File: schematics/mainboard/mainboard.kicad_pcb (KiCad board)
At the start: 4 copper layers, 92 x 166.8 mm, 82 parts, among them J1 SD_Card_Receptacle, J2 Conn_02x20_Odd_Even_MountingP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, J3 USB_C_Receptacle_USB2.0_16P, J4 Conn_01x02, J5 Conn_01x03_Pin, J6 Conn_01x12, P1 1-1473005-4, SW1 SW_SPST, U1 AMS1117-3.3, U2 AMS1117-3.3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

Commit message: SD card connector fixed in schematics. Added JLCPBC part numbers to some components.
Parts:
- added R29: 57k, Resistor_SMD:R_0805_2012Metric_Pad1.20x1.40mm_HandSolder, F.Cu at (124.0, 115.8)
- J1: footprint Connector_Card:SD_Hirose_DM1AA_SF_PEJ82 -> DM1AA-SF-PEJ(82):RetroDACK SD_Hirose_DM1AA_SF_PEJ82
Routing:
- net GND: track 183.4 -> 197.5 mm, vias 56 -> 60
- net SD_CARD: track 0.00 -> 4.69 mm
- net 3V3_LCD: track 148.5 -> 151.4 mm

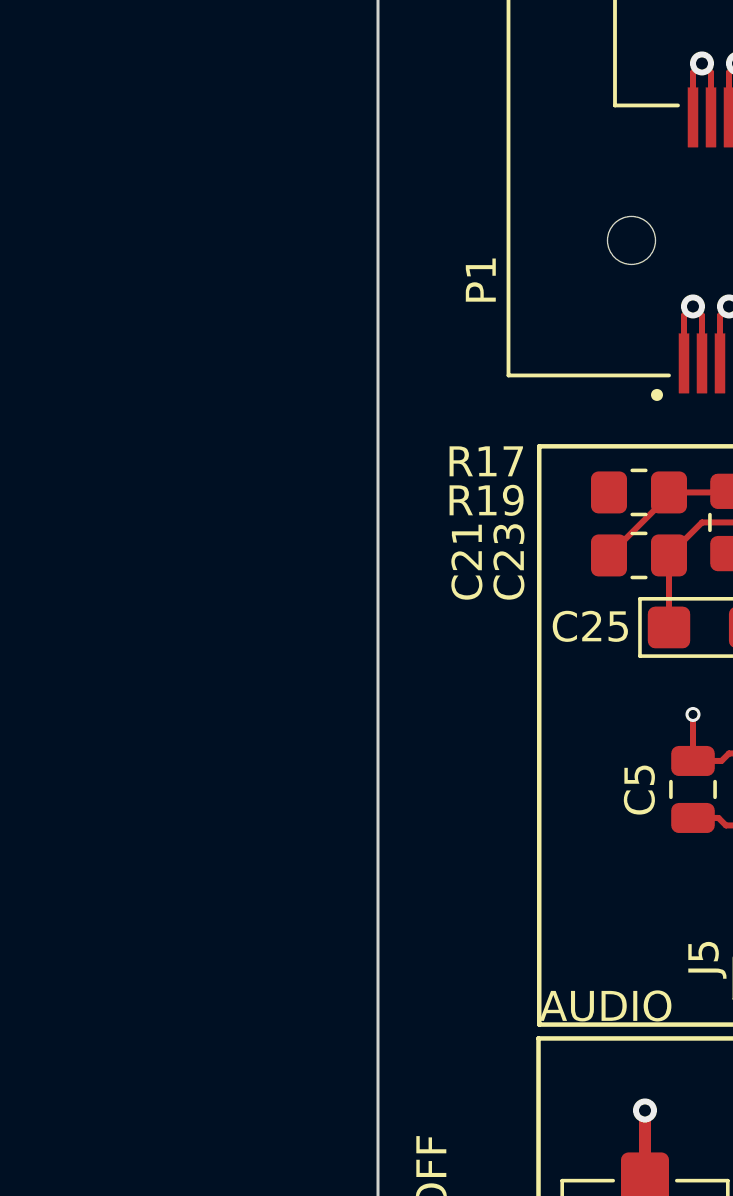
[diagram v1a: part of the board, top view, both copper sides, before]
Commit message: Added connector for trackball to mainboard schematics.
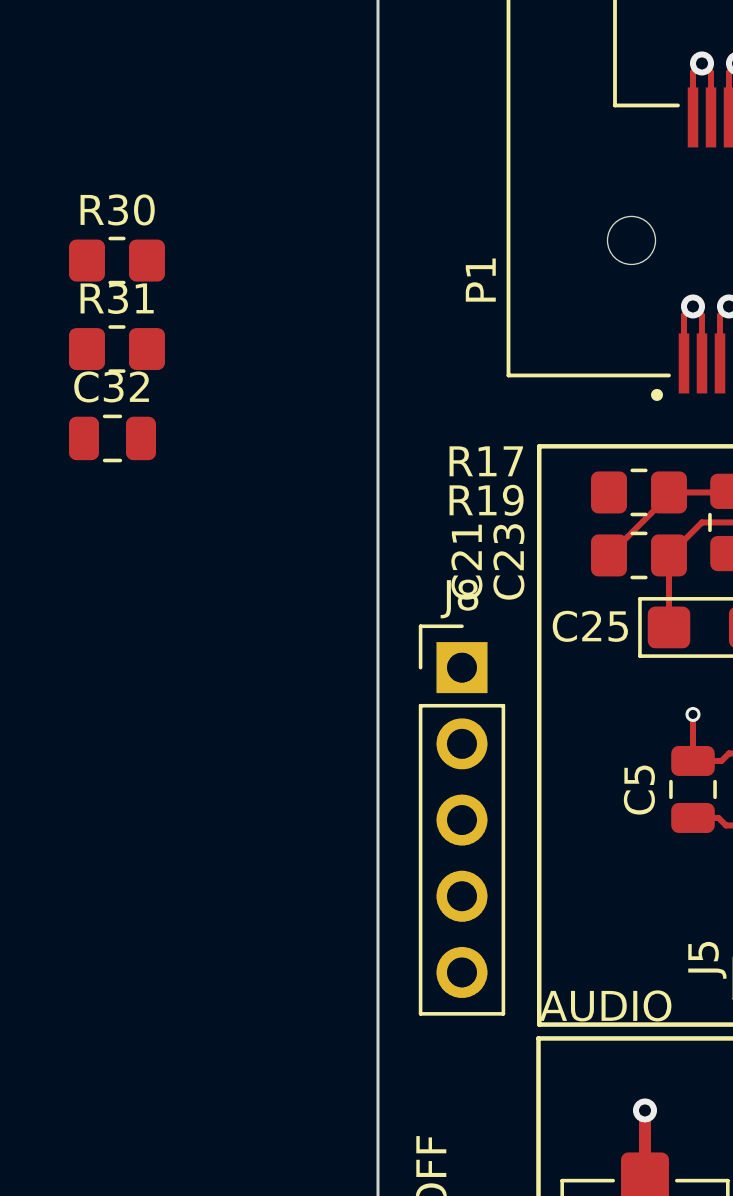
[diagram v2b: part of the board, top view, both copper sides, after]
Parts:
- added C32: 1uF, Capacitor_SMD:C_0805_2012Metric, F.Cu at (106.2, 201.5)
- added J8: TRACKBALL_CONN, Connector_PinHeader_2.54mm:PinHeader_1x05_P2.54mm_Vertical, F.Cu at (117.8, 209.1)
- added R30: 1k2, Resistor_SMD:R_0805_2012Metric_Pad1.20x1.40mm_HandSolder, F.Cu at (106.3, 195.6)
- added R31: 1k2, Resistor_SMD:R_0805_2012Metric_Pad1.20x1.40mm_HandSolder, F.Cu at (106.3, 198.5)
- J2: value Conn_02x20_Odd_Even_MountingPin -> LCD_CONN
- J4: value Conn_01x02 -> BATTERY_CONN
- J6: value Conn_01x12 -> HID_CONN
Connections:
- P1 pad 58: unconnected-(P1-Pad58) -> I2C_SCL
- P1 pad 60: unconnected-(P1-Pad60) -> I2C_SDA
- P1 pad 62: unconnected-(P1-Pad62) -> I2C_INTERRUPT

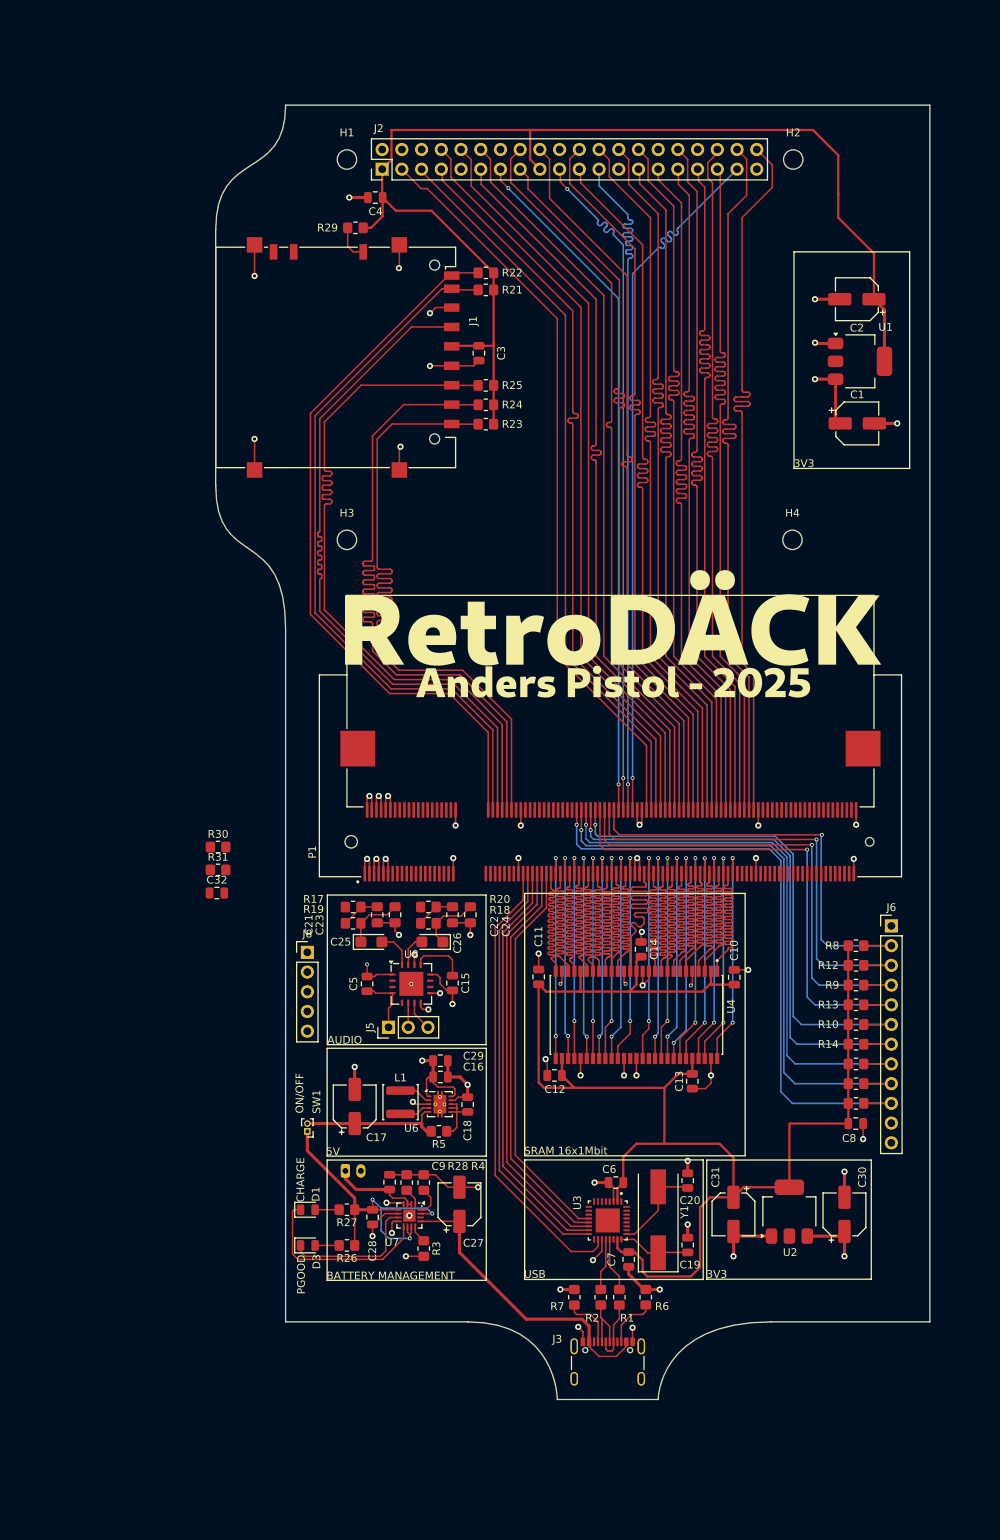
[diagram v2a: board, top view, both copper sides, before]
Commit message: Updated mainboard to use I2S audio.
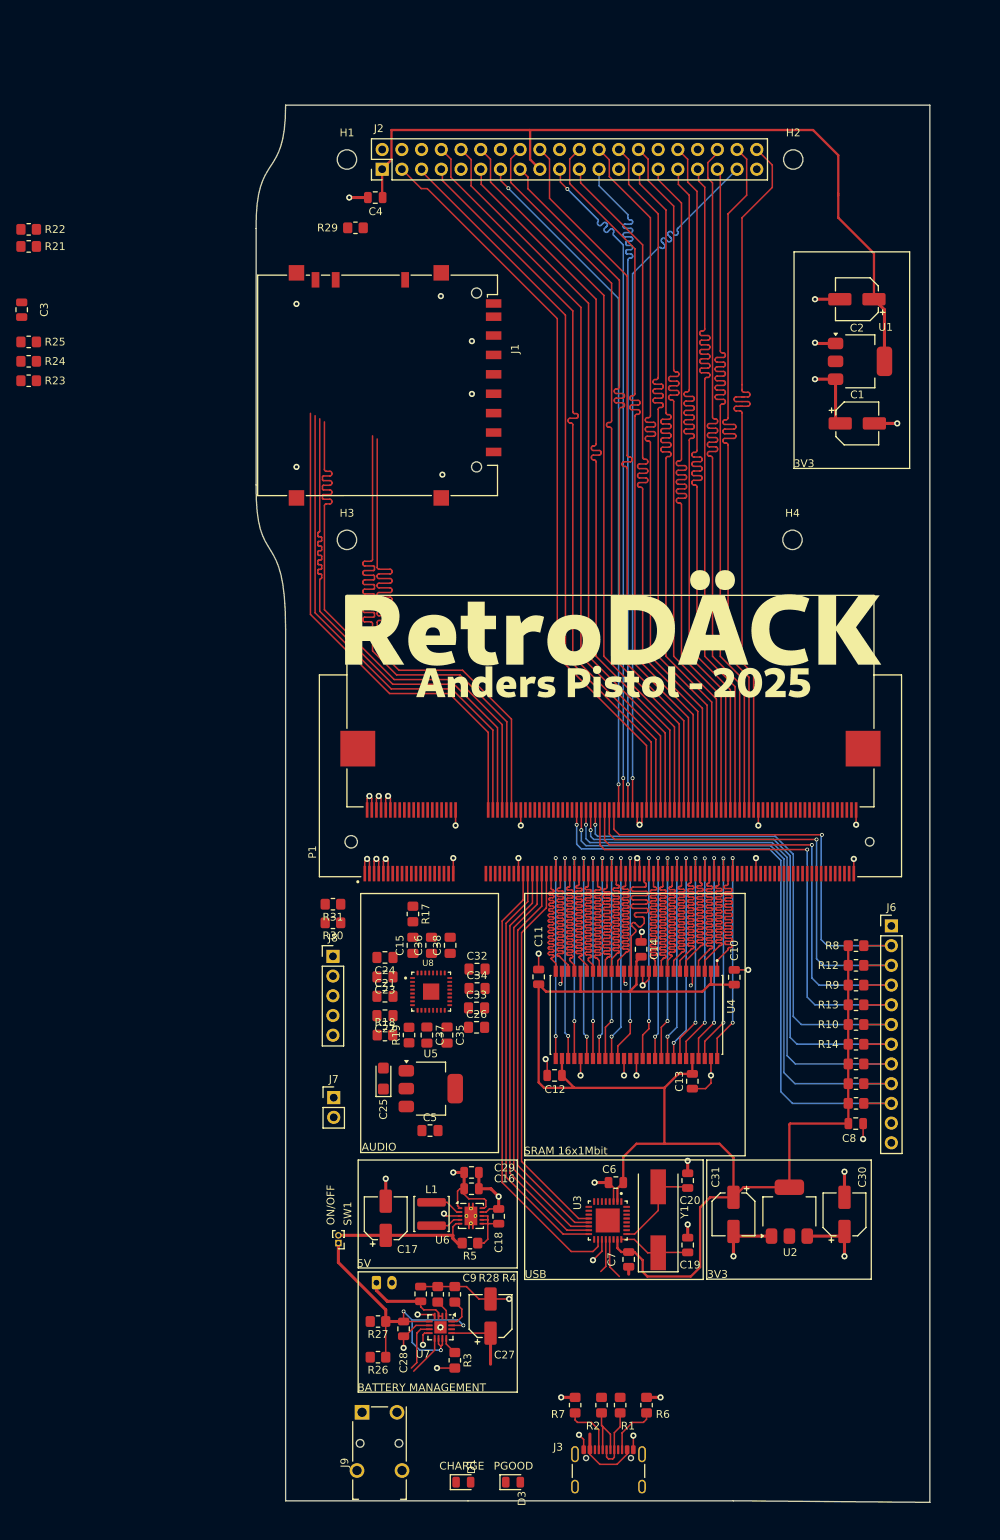
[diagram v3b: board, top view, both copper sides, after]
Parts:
- removed J5: Conn_01x03_Pin, Connector_PinHeader_2.54mm:PinHeader_1x03_P2.54mm_Vertical
- removed R20: 4k7, Resistor_SMD:R_0805_2012Metric_Pad1.20x1.40mm_HandSolder
- added C33: 10uF, Capacitor_SMD:C_0805_2012Metric_Pad1.18x1.45mm_HandSolder, F.Cu at (139.6, 216.3)
- added C34: 22uF, Capacitor_SMD:C_0805_2012Metric_Pad1.18x1.45mm_HandSolder, F.Cu at (139.7, 213.8)
- added C35: 0.1uF, Capacitor_SMD:C_0805_2012Metric_Pad1.18x1.45mm_HandSolder, F.Cu at (135.8, 219.8)
- added C36: 0.1uF, Capacitor_SMD:C_0805_2012Metric_Pad1.18x1.45mm_HandSolder, F.Cu at (133.8, 208.2)
- added C37: 10uF, Capacitor_SMD:C_0805_2012Metric_Pad1.18x1.45mm_HandSolder, F.Cu at (133.2, 219.8)
- added C38: 22uF, Capacitor_SMD:C_0805_2012Metric_Pad1.18x1.45mm_HandSolder, F.Cu at (136.2, 208.2)
- added J7: Conn_01x02_Pin, Connector_PinHeader_2.54mm:PinHeader_1x02_P2.54mm_Vertical, F.Cu at (121.2, 227.9)
- added J9: AudioJack3, Connector_Audio:Jack_3.5mm_Switronic_ST-005-G_horizontal, F.Cu at (127.1, 274.9)
- added U5: AMS1117-1.8, Package_TO_SOT_SMD:SOT-223-3_TabPin2, F.Cu at (133.7, 226.7)
- C15, C32: value 1uF -> 0.1uF; footprint Capacitor_SMD:C_0805_2012Metric -> Capacitor_SMD:C_0805_2012Metric_Pad1.18x1.45mm_HandSolder
- C21, C23: value 10nF -> 0.1uF
- C22, C24: value 10nF -> 10uF
- C26: value 47uF -> 0.1uF; footprint Capacitor_Tantalum_SMD:CP_EIA-3216-18_Kemet-A -> Capacitor_SMD:C_0805_2012Metric_Pad1.18x1.45mm_HandSolder
- C5: value 1uF -> 10uF; footprint Capacitor_SMD:C_0805_2012Metric -> Capacitor_SMD:C_0805_2012Metric_Pad1.18x1.45mm_HandSolder
- U8: value MAX9715xTE+ -> ~; footprint Package_DFN_QFN:TQFN-16-1EP_5x5mm_P0.8mm_EP3.1x3.1mm -> MY_AUDIO:QFN50P500X500X100-33N
- moved C3 59.2 mm to (81.0, 126.3)
- moved R21 59.2 mm to (81.9, 118.2)
- moved R22 59.2 mm to (81.9, 116.0)
- moved R23 59.2 mm to (81.9, 135.5)
- moved R24 59.2 mm to (81.9, 133.0)
- moved R25 59.2 mm to (81.9, 130.5)
- moved D1 40.4 mm to (137.9, 277.4)
- moved D3 40.4 mm to (144.3, 277.4)
- moved C32 34.9 mm to (139.7, 211.3)
- moved C5 20.6 mm to (133.6, 232.1), turned to 0 degrees
- moved R30 17.7 mm to (121.1, 205.3), turned to 180 degrees
- moved C25 17.7 mm to (127.6, 225.4), turned to 90 degrees
- moved R18 17.4 mm to (127.8, 219.8)
- moved R19 16.1 mm to (130.9, 219.8), turned to 90 degrees
- moved C22 15.6 mm to (127.8, 217.3), turned to 180 degrees
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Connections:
- net Net-(U8-OUTR+) renamed VOL/MICDET
- C15 pad 1: Net-(U8-BIAS) -> ~{RESET}
- C2 pad 1: 3V3_LCD -> 3V3_AUDIO
- C21 pad 1: Net-(C21-Pad1) -> 1V8
- C22 pad 1: GND -> 1V8
- C22 pad 2: Net-(C22-Pad2) -> GND
- C23 pad 1: Net-(C23-Pad1) -> 3V3_AUDIO
- C24 pad 1: GND -> 3V3_AUDIO
- C24 pad 2: Net-(C24-Pad2) -> GND
- C25 pad 1: Net-(C23-Pad1) -> 1V8
- C25 pad 2: Net-(U8-INL) -> GND
- C26 pad 1: Net-(C24-Pad2) -> 3V3_AUDIO
- C26 pad 2: Net-(U8-INR) -> GND
- C3 pad 2: 3V3_LCD -> 3V3_AUDIO
- C32 pad 1: GND -> 5V0
- C32 pad 2: 5V0 -> GND
- C4 pad 2: 3V3_LCD -> 3V3_AUDIO
- C5 pad 1: GND -> 3V3_AUDIO
- C5 pad 2: 5V0 -> GND
- J1 pad 4: 3V3_LCD -> 3V3_AUDIO
- J2 pad 1: 3V3_LCD -> 3V3_AUDIO
- J2 pad 17: 3V3_LCD -> 3V3_AUDIO
- R17 pad 1: PWM_L -> 3V3_AUDIO
- R17 pad 2: Net-(C21-Pad1) -> ~{RESET}
- R18 pad 1: PWM_R -> 3V3_AUDIO
- R18 pad 2: Net-(C22-Pad2) -> AUDIO_SDA
- R19 pad 1: Net-(C21-Pad1) -> 3V3_AUDIO
- R19 pad 2: Net-(C23-Pad1) -> AUDIO_SCL
- R21 pad 2: 3V3_LCD -> 3V3_AUDIO
- R22 pad 2: 3V3_LCD -> 3V3_AUDIO
- R23 pad 2: 3V3_LCD -> 3V3_AUDIO
- R24 pad 2: 3V3_LCD -> 3V3_AUDIO
- R25 pad 2: 3V3_LCD -> 3V3_AUDIO
- R29 pad 2: 3V3_LCD -> 3V3_AUDIO
- U1 pad 2: 3V3_LCD -> 3V3_AUDIO
- U8 pad 10: Net-(U8-OUTR-) -> AUDIO_SCL
- U8 pad 12: GND -> unconnected-(U8-MICBIAS-Pad12)
- U8 pad 13: Net-(U8-BIAS) -> GND
- U8 pad 14: 5V0 -> GND
- U8 pad 15: Net-(U8-INR) -> unconnected-(U8-NC-Pad15)
- U8 pad 16: Net-(U8-INL) -> GND
- U8 pad 17: GND -> 3V3_AUDIO
- U8 pad 2: Net-(U8-OUTL+) -> 3V3_AUDIO
- U8 pad 3: Net-(U8-OUTL-) -> 1V8
- U8 pad 4: 5V0 -> unconnected-(U8-NC-Pad4)
- U8 pad 5: unconnected-(U8-NC-Pad5) -> AUDIO_DIN
- U8 pad 6: Net-(J5-Pin_2) -> AUDIO_WCLK
- U8 pad 7: GND -> AUDIO_BCLK
- U8 pad 8: 5V0 -> AUDIO_MCLK
- U8 pad 9: 5V0 -> AUDIO_SDA
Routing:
- net 3V3_LCD: track 151.4 -> 0.00 mm
- net 3V3_AUDIO: track 0.00 -> 102.8 mm
- net GND: track 197.5 -> 148.3 mm, vias 60 -> 55
- net SD_DAT1: track 94.2 -> 65.1 mm
- net SD_DAT0: track 92.7 -> 64.9 mm
- net SD_CLK: track 90.1 -> 68.2 mm
- net SD_CMD: track 93.6 -> 71.9 mm
- net USB_VBUS: track 38.7 -> 18.1 mm
- net Net-(D1-K): track 23.8 -> 5.33 mm
- net SD_DAT3: track 93.4 -> 78.1 mm
- net SD_DAT2: track 93.7 -> 79.9 mm
- net 5V0: track 52.7 -> 40.4 mm, vias 9 -> 6
- net Net-(D3-K): track 17.9 -> 6.61 mm
- net Net-(C24-Pad2): track 8.04 -> 0.00 mm
- net Net-(C23-Pad1): track 7.69 -> 0.00 mm
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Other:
- board size 92 x 166.8 mm -> 86.8 x 180 mm

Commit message: Mainboard work, trying to figure out optimal outline.
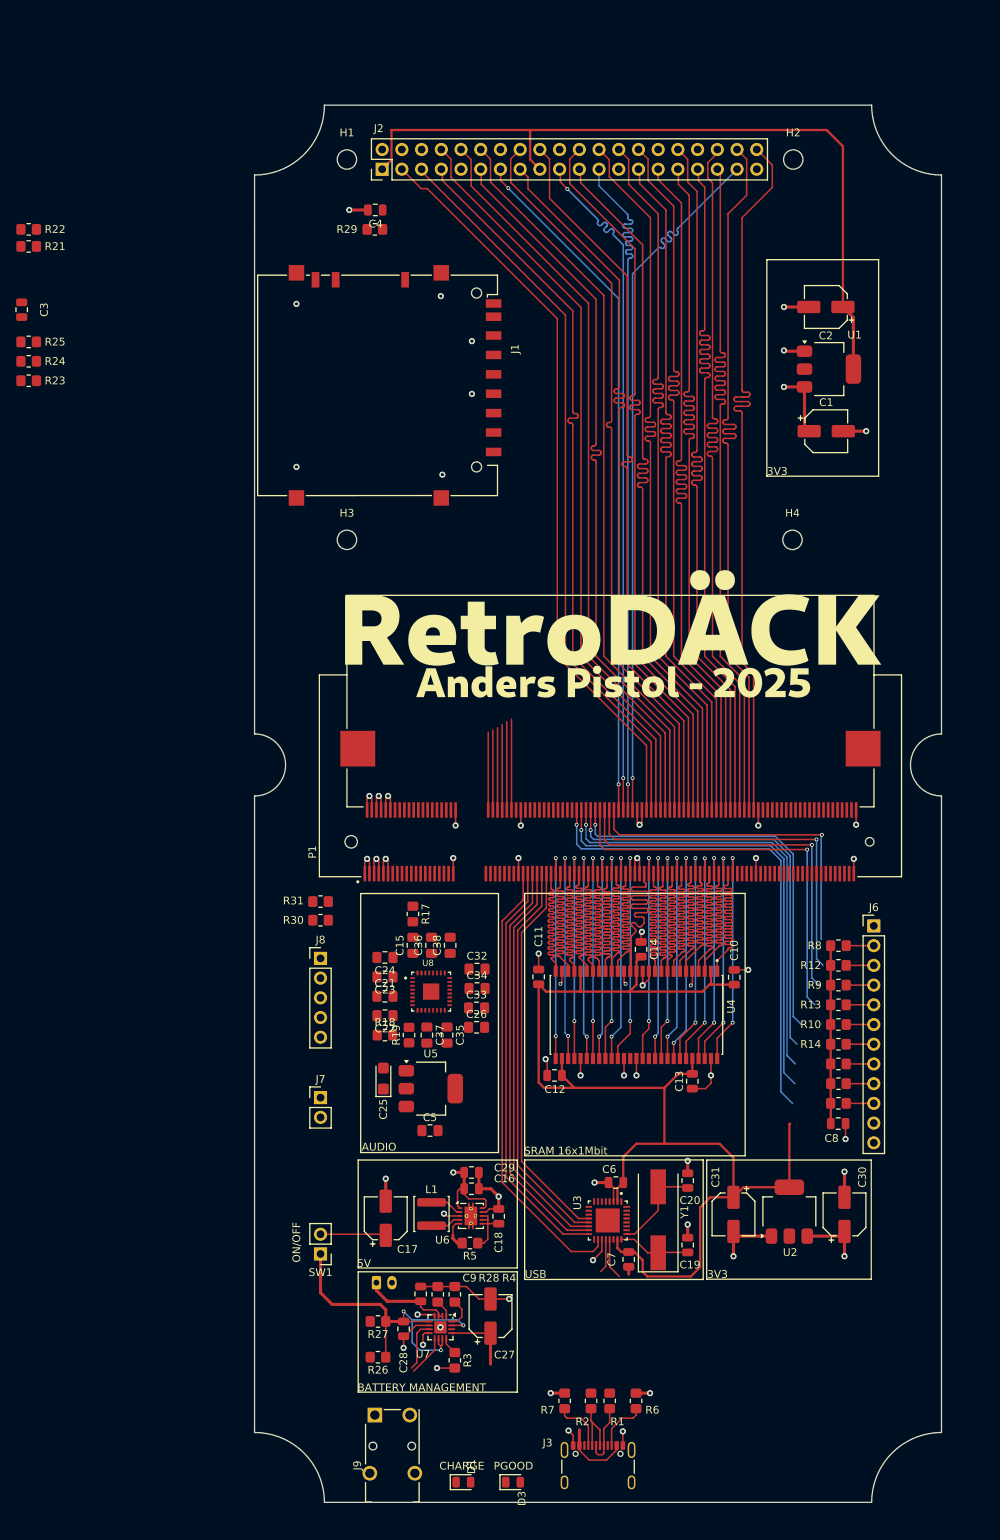
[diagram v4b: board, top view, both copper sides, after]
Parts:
- J7: value Conn_01x02_Pin -> SPEAKER
- SW1: footprint Connector_PinHeader_1.00mm:PinHeader_1x02_P1.00mm_Vertical -> Connector_PinHeader_2.54mm:PinHeader_1x02_P2.54mm_Vertical
- moved C1 4.12 mm to (184.7, 142.0)
- moved C2 4.12 mm to (184.6, 126.0)
- moved U1 4.12 mm to (185.0, 134.0)
- moved SW1 2.69 mm to (119.5, 248.0)
- moved R29 2.51 mm to (126.5, 116.0)
- moved C8 2.26 mm to (186.2, 231.2)
- moved J6 2.26 mm to (190.8, 205.7)
- moved R10 2.26 mm to (186.2, 218.4)
- moved R11 2.26 mm to (186.2, 223.5)
- moved R12 2.26 mm to (186.2, 210.8)
- moved R13 2.26 mm to (186.2, 215.9)
- moved R14 2.26 mm to (186.2, 221.0)
- moved R15 2.26 mm to (186.2, 226.1)
- moved R16 2.26 mm to (186.2, 228.6)
- moved R8 2.26 mm to (186.2, 208.3)
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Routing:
- net SD_DAT2: track 79.9 -> 11.7 mm
- net SD_DAT3: track 78.1 -> 11.4 mm
- net SD_CMD: track 71.9 -> 11.0 mm
- net SD_CLK: track 68.2 -> 10.6 mm
- net SD_DAT1: track 65.1 -> 10.0 mm
- net SD_DAT0: track 64.9 -> 10.3 mm
- net HIO_BTN_X: track 79.8 -> 67.0 mm
- net HIO_BTN_D: track 76.6 -> 64.2 mm
- net HIO_BTN_C: track 73.6 -> 61.2 mm
- net HIO_BTN_B: track 70.5 -> 58.3 mm
- net HIO_BTN_A: track 67.2 -> 55.6 mm
- net HIO_DPAD_E: track 65.3 -> 55.4 mm
- net HIO_DPAD_N: track 56.1 -> 46.7 mm
- net HIO_DPAD_W: track 62.2 -> 52.8 mm
- net HIO_DPAD_S: track 59.0 -> 50.2 mm
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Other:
- board size 86.8 x 180 mm -> 88.5 x 180 mm
